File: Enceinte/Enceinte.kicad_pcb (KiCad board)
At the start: 4 copper layers, 51 x 22 mm, 49 parts, among them IC1 TPA3110D2PWPR, J1 Conn_01x07, J10 Conn_01x03, J11 Conn_01x03, J2 Conn_01x02, J3 Conn_01x02, J4 Conn_01x02, J5 Conn_01x02, J6 Conn_01x05, J7 Conn_01x06, J8 Conn_01x02, J9 Conn_01x02, U1 173010342

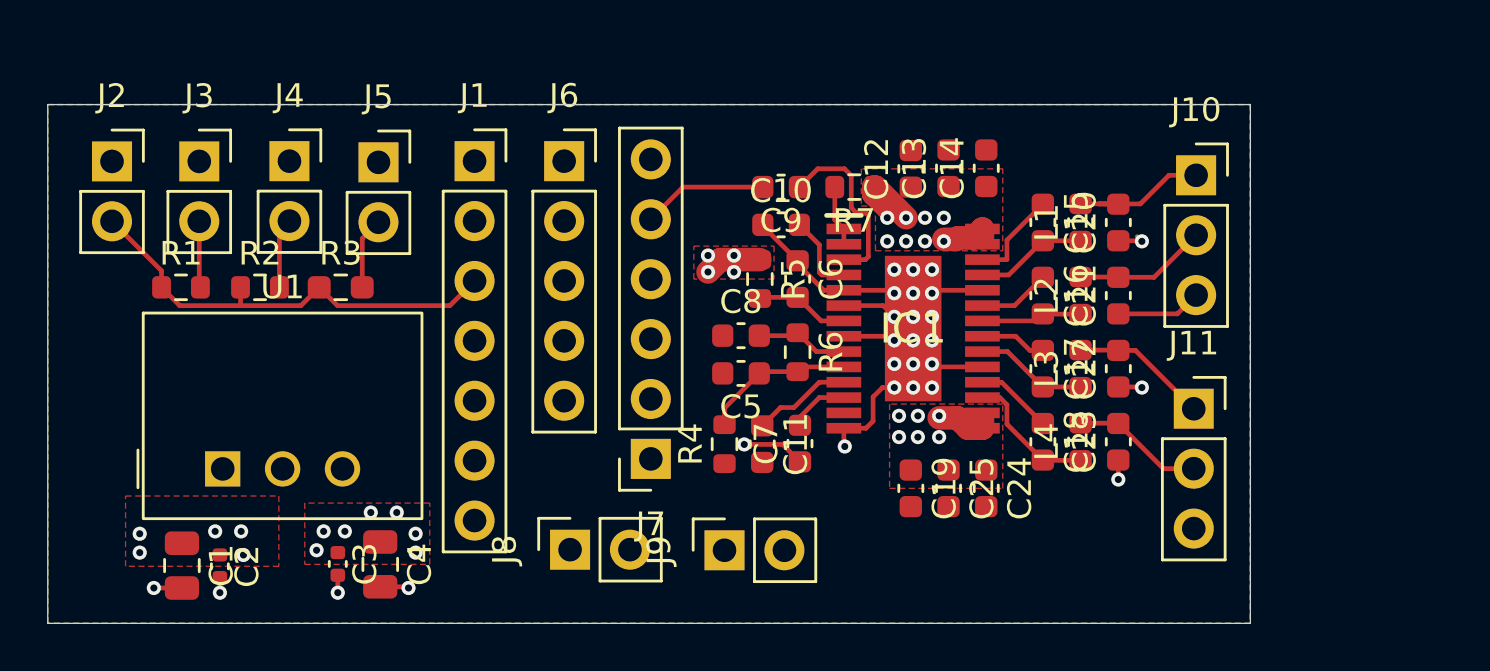
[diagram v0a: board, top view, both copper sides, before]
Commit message: Changement régulateur de tension
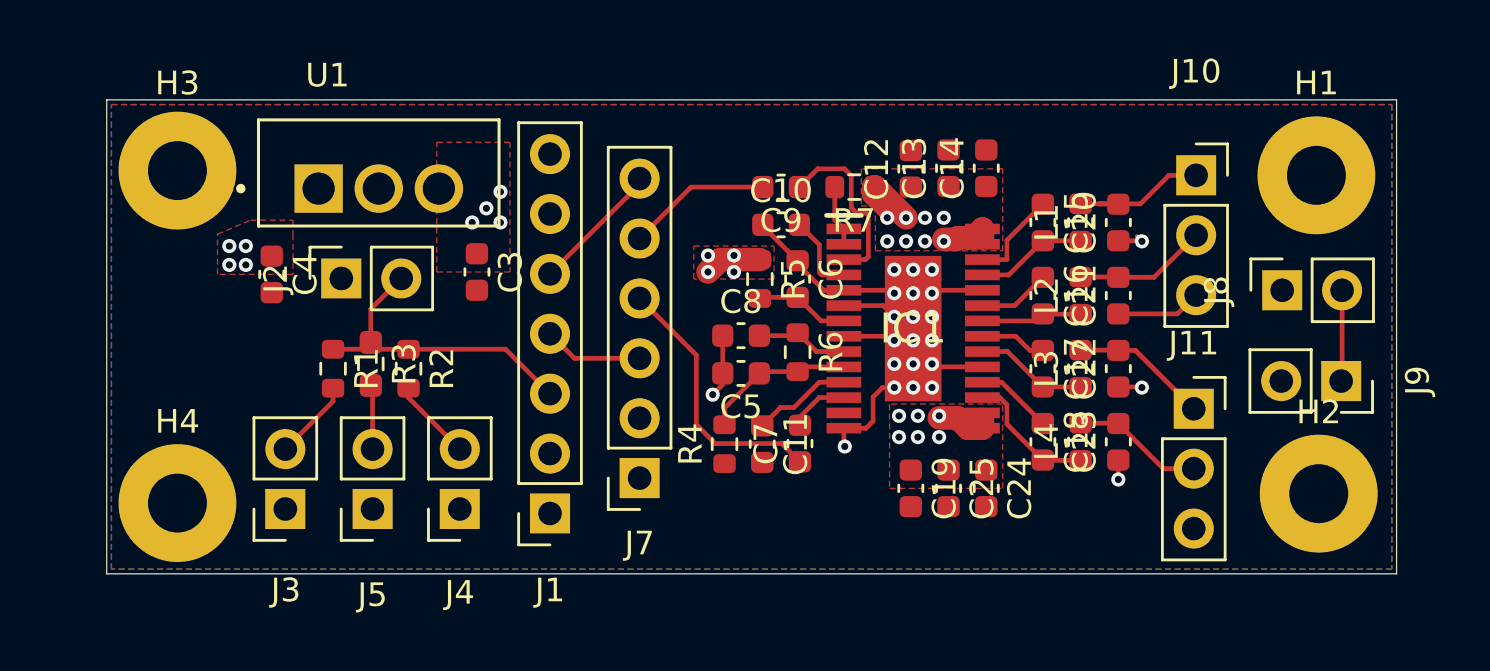
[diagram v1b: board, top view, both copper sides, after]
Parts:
- removed C1: 4u7, Capacitor_SMD:C_0805_2012Metric
- removed C2: 100 n, Capacitor_SMD:C_0402_1005Metric
- removed J6: Conn_01x05, Connector_PinSocket_2.54mm:PinSocket_1x05_P2.54mm_Vertical
- added H1: MountingHole_Pad, MountingHole:MountingHole_2.5mm_Pad, F.Cu at (152.8, 58.0)
- added H2: MountingHole_Pad, MountingHole:MountingHole_2.5mm_Pad, F.Cu at (152.9, 71.5)
- added H3: MountingHole_Pad, MountingHole:MountingHole_2.5mm_Pad, F.Cu at (104.5, 57.8)
- added H4: MountingHole_Pad, MountingHole:MountingHole_2.5mm_Pad, F.Cu at (104.5, 71.9)
- C3: value 100 n -> 0.1u; footprint Capacitor_SMD:C_0402_1005Metric -> Capacitor_SMD:C_0603_1608Metric
- C4: value 4u7 -> 0.33u; footprint Capacitor_SMD:C_0805_2012Metric -> Capacitor_SMD:C_0603_1608Metric
- U1: value 173010342 -> L7805; footprint MagIC_THT_Wurth:U_Wurth_MagIC-FDSM_173010x42 -> L7805:TO255P1020X450X2000-3
- moved J8 32.1 mm to (151.3, 62.9)
- moved J9 27.1 mm to (153.8, 66.7), turned to -90 degrees
- moved J4 16.4 mm to (116.5, 72.2), turned to 180 degrees
- moved J1 15.3 mm to (120.3, 72.3), turned to 180 degrees
- moved J3 15.2 mm to (109.1, 72.2), turned to 180 degrees
- moved J5 14.7 mm to (112.8, 72.2), turned to 180 degrees
- moved U1 14.2 mm to (113.0, 57.9)
- moved C3 13.7 mm to (117.2, 62.1)
- moved C4 13.1 mm to (108.5, 62.2)
- moved J2 10.9 mm to (111.5, 62.4), turned to 90 degrees
- moved R1 7.31 mm to (111.1, 66.2), turned to -90 degrees
- moved R2 7.18 mm to (114.3, 66.2), turned to -90 degrees
- moved R3 3.49 mm to (112.7, 66.0), turned to -90 degrees
- moved J7 0.94 mm to (124.1, 70.8)
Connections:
- C4 pad 1: +5V -> +12V
- J1 pad 4: /BT D -> /In_Pot_R
- J1 pad 5: /BT G -> /In_Pot_L
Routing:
- net /BT G: track 6.65 -> 0.00 mm
- net Net-(J1-Pin_3): track 19.1 -> 13.5 mm
- net /BT D: track 3.80 -> 0.00 mm
- net /In_Pot_L: track 4.76 -> 5.61 mm
- net GND: track 30.7 -> 29.9 mm, vias 26 -> 23
- net /TPA3110D2PWPR/Pot_L: track 5.32 -> 6.13 mm
- net Net-(J3-Pin_2): track 2.82 -> 3.42 mm
- net /In_Pot_R: track 4.76 -> 4.23 mm
- net /TPA3110D2PWPR/Pot_R: track 11.3 -> 11.4 mm, vias 1 -> 0
- net +5V: vias 7 -> 4
- net +12V: vias 23 -> 22
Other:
- board size 51 x 22 mm -> 54.7 x 20.1 mm

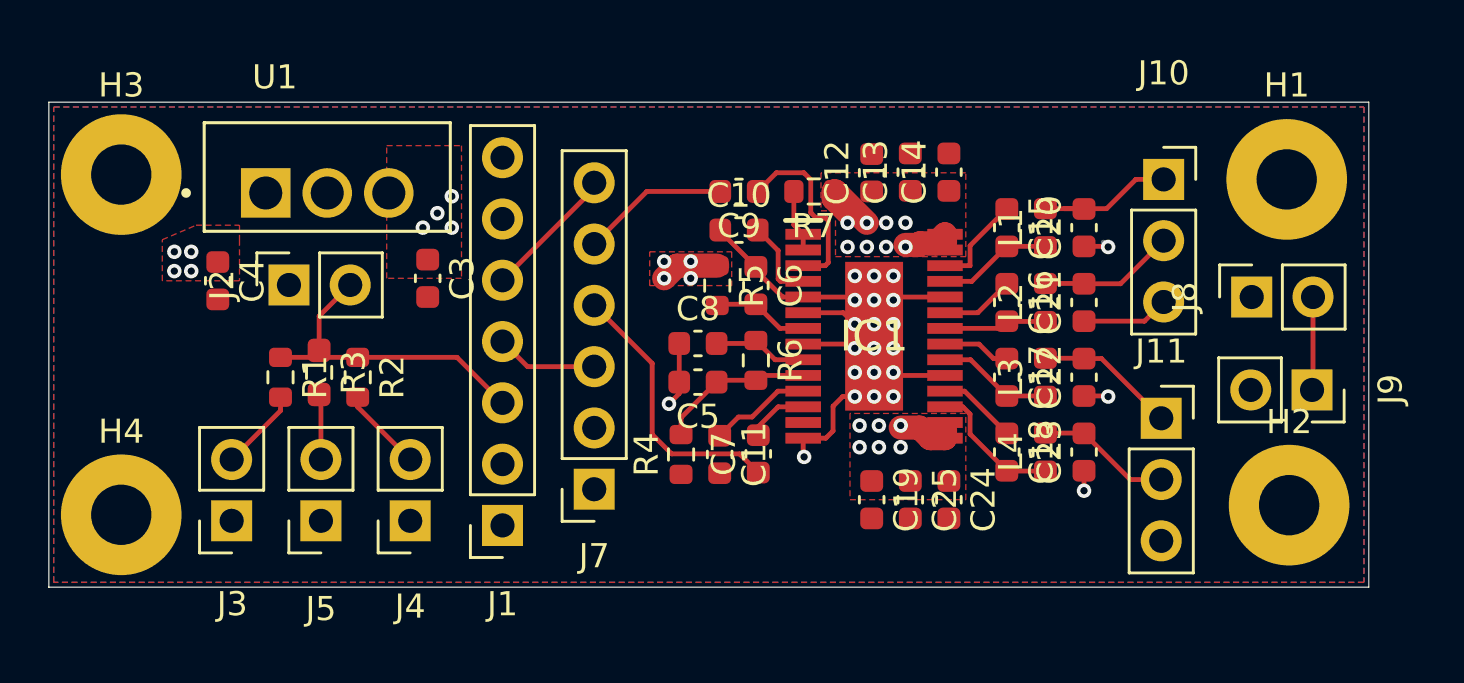
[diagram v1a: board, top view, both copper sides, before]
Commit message: correction des bordures
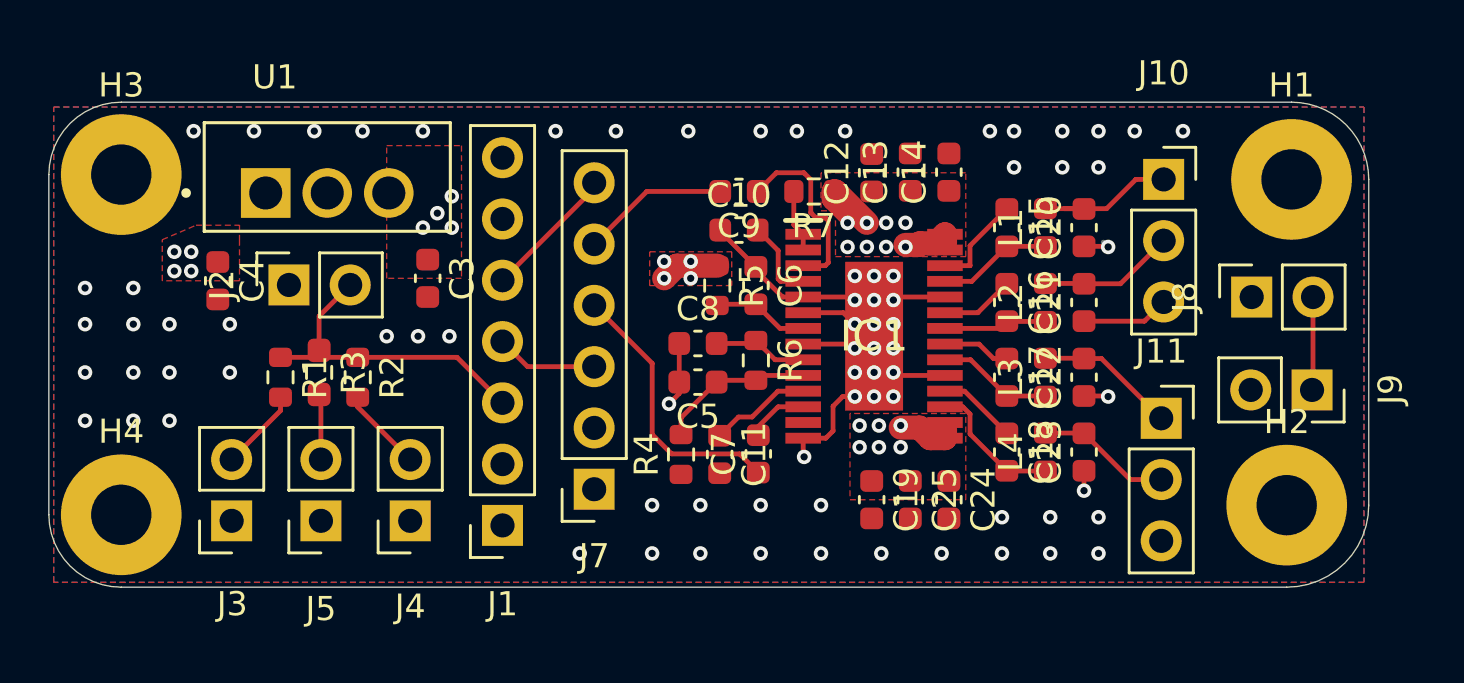
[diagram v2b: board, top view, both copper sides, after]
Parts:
- moved H1 0.20 mm to (153.0, 58.0)
- moved H2 0.10 mm to (152.8, 71.5)
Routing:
- net GND: vias 23 -> 76
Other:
- outline, holes or cut-outs redrawn

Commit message: des changements sont à faire
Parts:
- C12, C19: footprint Capacitor_SMD:C_0603_1608Metric -> Capacitor_SMD:CP_Elec_6.3x7.7
- moved C19 28.0 mm to (123.2, 46.2)
- moved C12 12.0 mm to (131.4, 46.5)

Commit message: doc latex
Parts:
- removed the C12 at (131.4, 46.5)
- removed the C19 at (123.2, 46.2)
- removed J11: Conn_01x03, Connector_PinSocket_2.54mm:PinSocket_1x03_P2.54mm_Vertical
- added C1: 100n, Capacitor_SMD:C_0603_1608Metric, F.Cu at (94.3, 114.5)
- added C14: 220u, Capacitor_SMD:CP_Elec_6.3x7.7, F.Cu at (124.2, 100.2)
- added C2: 4u7, Capacitor_SMD:C_0603_1608Metric, F.Cu at (92.7, 114.5)
- added C21: 220u, Capacitor_SMD:CP_Elec_6.3x7.7, F.Cu at (124.7, 124.3)
- added C5: 100 n, Capacitor_SMD:C_0603_1608Metric, F.Cu at (97.8, 98.7)
- added C6: 4u7, Capacitor_SMD:C_0603_1608Metric, F.Cu at (100.0, 98.6)
- added D1: LED, LED_SMD:LED_0603_1608Metric, F.Cu at (90.4, 98.2)
- added J6: Conn_01x02, Connector_JST:JST_XH_B2B-XH-A_1x02_P2.50mm_Vertical, F.Cu at (86.1, 105.2)
- added L1: 100n, Inductor_SMD:L_0603_1608Metric, F.Cu at (95.9, 114.5)
- added R8: 1k, Resistor_SMD:R_0402_1005Metric, F.Cu at (90.7, 100.0)
- added TP1: TestPoint, TestPoint:TestPoint_Pad_D1.5mm, F.Cu at (95.2, 98.6)
- added TP3: TestPoint, TestPoint:TestPoint_Pad_D1.5mm, F.Cu at (133.8, 101.7)
- added TP4: TestPoint, TestPoint:TestPoint_Pad_D1.5mm, F.Cu at (132.1, 104.0)
- added TP5: TestPoint, TestPoint:TestPoint_Pad_D1.5mm, F.Cu at (133.6, 120.3)
- added TP6: TestPoint, TestPoint:TestPoint_Pad_D1.5mm, F.Cu at (133.6, 123.3)
- C3: value 0.1u -> 4u7
- C4: value 0.33u -> 100 n
- J1: value Conn_01x07 -> Conn_01x06; footprint Connector_PinSocket_2.54mm:PinSocket_1x07_P2.54mm_Vertical -> Connector_JST:JST_XH_B6B-XH-A_1x06_P2.50mm_Vertical
- J10: footprint Connector_PinSocket_2.54mm:PinSocket_1x03_P2.54mm_Vertical -> Connector_JST:JST_XH_B3B-XH-A_1x03_P2.50mm_Vertical
- J2, J3, J4, J5: footprint Connector_PinSocket_2.54mm:PinSocket_1x02_P2.54mm_Vertical -> Connector_JST:JST_XH_B2B-XH-A_1x02_P2.50mm_Vertical
- J7: value Conn_01x06 -> Conn_01x02; footprint Connector_PinSocket_2.54mm:PinSocket_1x06_P2.54mm_Vertical -> Connector_JST:JST_XH_B2B-XH-A_1x02_P2.50mm_Vertical
- J8: value Conn_01x02 -> Conn_01x06; footprint Connector_PinSocket_2.54mm:PinSocket_1x02_P2.54mm_Vertical -> Connector_JST:JST_XH_B6B-XH-A_1x06_P2.50mm_Vertical
- J9: value Conn_01x02 -> Conn_01x03; footprint Connector_PinSocket_2.54mm:PinSocket_1x02_P2.54mm_Vertical -> Connector_JST:JST_XH_B3B-XH-A_1x03_P2.50mm_Vertical
- U1: value L7805 -> 173010342; footprint L7805:TO255P1020X450X2000-3 -> MagIC_THT_Wurth:U_Wurth_MagIC-FDSM_173010x42
- moved J8 64.4 mm to (112.0, 113.8)
- moved J2 64.0 mm to (116.0, 126.2)
- moved J10 58.4 mm to (139.1, 115.8), turned to -90 degrees
- moved H4 57.8 mm to (85.5, 126.5)
- moved H2 56.8 mm to (138.5, 126.5)
- moved J7 56.2 mm to (88.7, 114.5)
- moved J4 55.9 mm to (102.0, 126.2), turned to 90 degrees
- moved J3 55.8 mm to (95.0, 126.2), turned to 90 degrees
- moved C3 55.6 mm to (98.3, 114.4)
- moved R1 55.2 mm to (97.8, 119.8), turned to 0 degrees
- moved R2 54.9 mm to (102.2, 119.8), turned to 0 degrees
- moved J5 54.1 mm to (109.0, 126.2), turned to 90 degrees
- moved R3 54.0 mm to (107.4, 119.8), turned to 0 degrees
- moved U1 53.1 mm to (99.2, 109.2), turned to 90 degrees
- moved C4 52.9 mm to (100.0, 114.4)
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- renumbered C8 to C10, C9 to C11, C10 to C12, C11 to C13, C13 to C15, C14 to C16, C15 to C17, C16 to C18, C17 to C19, C18 to C20, C20 to C22, C21 to C23, C22 to C24, C23 to C25, C24 to C26, C25 to C27, C5 to C7, C6 to C8, C7 to C9, L1 to L2, L2 to L3, L3 to L4, L4 to L5
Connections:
- C22 pad 2: Net-(J10-Pin_1) -> Net-(J9-Pin_1)
- C23 pad 2: Net-(J10-Pin_2) -> Net-(J9-Pin_2)
- C24 pad 2: Net-(J11-Pin_1) -> Net-(J10-Pin_1)
- C25 pad 2: Net-(J11-Pin_2) -> Net-(J10-Pin_2)
- C3 pad 1: +5V -> Net-(U1-VIN)
- C4 pad 1: +12V -> Net-(U1-VIN)
- J1 pad 1: GND -> Net-(J1-Pin_1)
- J1 pad 2: GND -> unconnected-(J1-Pin_2-Pad2)
- J1 pad 3: Net-(J1-Pin_3) -> +5V
- J1 pad 4: /In_Pot_R -> GND
- J1 pad 6: unconnected-(J1-Pin_6-Pad6) -> /In_Pot_R
- J2 pad 2: Net-(J1-Pin_3) -> Net-(J1-Pin_1)
- J7 pad 1: GND -> Net-(J6-Pin_2)
- J8 pad 1: +12V -> GND
- J8 pad 2: Net-(J8-Pin_2) -> GND
- J9 pad 1: Net-(J8-Pin_2) -> Net-(J9-Pin_1)
- J9 pad 2: GND -> Net-(J9-Pin_2)
- L2 pad 2: Net-(J10-Pin_1) -> Net-(J9-Pin_1)
- L3 pad 2: Net-(J10-Pin_2) -> Net-(J9-Pin_2)
- L4 pad 2: Net-(J11-Pin_1) -> Net-(J10-Pin_1)
- L5 pad 2: Net-(J11-Pin_2) -> Net-(J10-Pin_2)
- R1 pad 1: Net-(J1-Pin_3) -> Net-(J1-Pin_1)
- R2 pad 1: Net-(J1-Pin_3) -> Net-(J1-Pin_1)
- R3 pad 1: Net-(J1-Pin_3) -> Net-(J1-Pin_1)
- U1 pad 1: +12V -> Net-(U1-VIN)
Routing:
- net Net-(J1-Pin_1): track 0.00 -> 44.0 mm
- net Net-(J9-Pin_2): track 0.00 -> 16.1 mm, vias 0 -> 1
- net Net-(J9-Pin_1): track 0.00 -> 14.1 mm
- net Net-(J1-Pin_3): track 13.5 -> 0.00 mm
- net Net-(J10-Pin_2): track 5.64 -> 15.0 mm
- net Net-(J6-Pin_2): track 0.00 -> 9.32 mm
- net Net-(J10-Pin_1): track 6.21 -> 15.1 mm, vias 0 -> 1
- net Net-(U1-VIN): track 0.00 -> 8.84 mm
- net /In_Pot_L: track 5.61 -> 12.5 mm
- net /TPA3110D2PWPR/Pot_R: track 11.4 -> 17.7 mm
- net Net-(J11-Pin_1): track 5.83 -> 0.00 mm
- net Net-(J11-Pin_2): track 5.60 -> 0.00 mm
- net Net-(J8-Pin_2): track 3.87 -> 0.00 mm
- net /In_Pot_R: track 4.23 -> 8.07 mm
- net GND: track 29.9 -> 27.9 mm, vias 76 -> 25
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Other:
- board size 54.7 x 20.1 mm -> 60 x 35 mm

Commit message: nouvelles inductances
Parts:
- L1: footprint Inductor_SMD:L_0603_1608Metric -> Library_inductance_new:CWF1612A100J
- L2, L3, L4, L5: footprint Inductor_SMD:L_0603_1608Metric -> Library_inductance_new:SRN5040
- moved TP4 5.71 mm to (132.5, 98.3)
- moved H1 5.20 mm to (143.7, 98.5)
- moved H2 5.00 mm to (143.5, 126.7)
- moved L2 4.92 mm to (134.5, 103.2)
- moved TP5 4.82 mm to (138.4, 119.9)
- moved TP6 4.73 mm to (138.3, 122.8)
- moved J10 4.63 mm to (143.7, 115.6)
- moved J9 4.60 mm to (143.7, 104.4)
- moved L5 4.21 mm to (134.5, 120.7)
- moved TP3 4.18 mm to (136.6, 98.6)
- moved C22 4.04 mm to (138.1, 107.1)
- moved C23 4.04 mm to (138.1, 110.2)
- moved C24 4.04 mm to (138.1, 113.3)
- moved C25 4.04 mm to (138.1, 116.4)
- moved L3 2.76 mm to (134.5, 108.9)
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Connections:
- H1 pad 1: unconnected-(H1-Pad1) -> GND
- H2 pad 1: unconnected-(H2-Pad1) -> GND
- H3 pad 1: unconnected-(H3-Pad1) -> GND
- H4 pad 1: unconnected-(H4-Pad1) -> GND
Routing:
- net Net-(J9-Pin_2): track 16.1 -> 26.0 mm
- net Net-(J9-Pin_1): track 14.1 -> 22.4 mm
- net Net-(IC1-BSPR): track 5.75 -> 10.4 mm
- net Net-(J10-Pin_2): track 15.0 -> 19.3 mm
- net Net-(IC1-OUTPL): track 4.77 -> 8.86 mm
- net Net-(IC1-OUTNR): track 4.79 -> 7.54 mm
- net Net-(J10-Pin_1): track 15.1 -> 17.7 mm
- net Net-(IC1-BSNL): track 4.29 -> 6.65 mm
- net GND: track 27.9 -> 28.0 mm, vias 25 -> 116
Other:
- board size 60 x 35 mm -> 65 x 35 mm

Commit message: indu Wurth
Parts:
- removed TP1, TP3, TP4, TP5, TP6: TestPoint, TestPoint:TestPoint_Pad_D1.5mm
- L1: footprint Library_inductance_new:CWF1612A100J -> Inductor_SMD:L_Wuerth_HCI-5040
- L2, L3, L4, L5: footprint Library_inductance_new:SRN5040 -> Inductor_SMD:L_Wuerth_WE-PD-Typ-7345
- moved R2 4.78 mm to (107.0, 119.8)
- moved R1 4.77 mm to (102.6, 119.8), turned to 180 degrees
- moved R3 4.73 mm to (112.1, 119.1), turned to -90 degrees
- moved L5 4.07 mm to (136.2, 124.4), turned to 0 degrees
- moved L2 3.36 mm to (136.2, 100.3), turned to 0 degrees
- moved C22 3.34 mm to (141.4, 107.6)
- moved C23 3.34 mm to (141.4, 110.7)
- moved C24 3.34 mm to (141.4, 113.8)
- moved C25 3.34 mm to (141.4, 116.9)
- moved L1 3.29 mm to (94.9, 117.7), turned to -90 degrees
- moved J10 3.08 mm to (146.8, 115.8)
- moved J9 2.93 mm to (146.6, 104.5)
- moved C1 2.56 mm to (96.7, 113.5), turned to 180 degrees
- moved H2 2.50 mm to (146.0, 126.7)
- moved L4 2.40 mm to (136.2, 116.4), turned to 0 degrees
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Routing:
- net Net-(J9-Pin_2): track 26.0 -> 9.33 mm, vias 1 -> 0
- net Net-(J9-Pin_1): track 22.4 -> 13.7 mm
- net Net-(J1-Pin_1): track 44.0 -> 36.4 mm
- net Net-(J10-Pin_1): track 17.7 -> 10.8 mm, vias 1 -> 0
- net Net-(U1-VIN): track 8.96 -> 14.5 mm
- net Net-(IC1-OUTPL): track 8.86 -> 12.3 mm
- net Net-(J4-Pin_2): track 4.33 -> 7.56 mm
- net Net-(J10-Pin_2): track 19.3 -> 16.1 mm
- net Net-(J3-Pin_2): track 5.41 -> 8.51 mm
- net Net-(IC1-BSPR): track 10.4 -> 11.7 mm
- net Net-(IC1-OUTNR): track 7.54 -> 6.20 mm
- net Net-(J5-Pin_2): track 4.17 -> 5.26 mm
- net GND: track 28.0 -> 27.5 mm, vias 116 -> 107
- net +12V: vias 25 -> 24
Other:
- board size 65 x 35 mm -> 68 x 35 mm
